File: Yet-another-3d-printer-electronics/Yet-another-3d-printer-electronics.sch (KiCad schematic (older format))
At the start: 118 parts, among them CON1 SD_Card, P1 USB_B, P2 BEDTEMP, P3 ENDTEMP, P4 X-ENDSTOP, P5 Y-ENDSTOP, P6 Z-ENDSTOP, SW1 Switch_DPST, U1 FT230XS, U2 LPC1114FBD48/302, X1 CRYSTAL_SMD

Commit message: Update schematics and pro file
Signed-off-by: Mateusz Krawczuk <mat.krawczuk@gmail.com>
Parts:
- removed Q?: 2N7000, symbol Q_NMOS_GDS
- added Q1: 2N7000, TO_SOT_Packages_THT:TO-92_Horizontal1_Inline_Narrow_Oval, symbol Q_NMOS_SGD
- 100K1: renamed from 100K; footprint (none) -> Resistors_SMD:R_0805_HandSoldering
- 100K2, 100K3, 100K4: renamed from 100K?; footprint (none) -> Resistors_SMD:R_0805_HandSoldering
- C10, C11, C12, C9: renamed from C?; footprint (none) -> Capacitors_THT:CP_Radial_D5.0mm_P2.00mm
- C13: renamed from 10u/30V; value C -> 10u/30V; footprint (none) -> Capacitors_SMD:C_1206_HandSoldering
- C14, C15, C16: renamed from 10u/30V?; value C -> 10u/30V; footprint (none) -> Capacitors_SMD:C_1206_HandSoldering
- D1, D2: symbol LED -> LED-RESCUE-Yet-another-3d-printer-electronics
- D10, D4, D6, D8: renamed from D?; footprint (none) -> Diodes_THT:D_DO-41_SOD81_P2.54mm_Vertical_AnodeUp
- D11, D12, D13, D14, D15, D16, D17, D18, D19, D20, D21, D22, D23, D24, D25, D26, D27, D28, D29, D30, D31, D32, D33, D34, D35, D36, D37, D38, D39, D40, D41, D42: renamed from D?; footprint (none) -> Yet-another-3d-printer-electronics:DO-214AC(SMA)
- D3, D5, D7, D9: renamed from D?; footprint (none) -> LEDs:LED_0805; symbol LED -> LED-RESCUE-Yet-another-3d-printer-electronics
- P1: symbol USB_B -> USB_B-RESCUE-Yet-another-3d-printer-electronics
- P10, P12: renamed from P?; footprint (none) -> Connectors_JST:JST_XH_B02B-XH-A_02x2.50mm_Straight
- P11, P13, P14, P9: renamed from P?; footprint (none) -> Socket_Strips:Socket_Strip_Straight_2x03_Pitch2.54mm
- P15, P16, P17, P18: renamed from P?; footprint (none) -> Connectors_JST:JST_XH_B04B-XH-A_04x2.50mm_Straight
- P2, P3: footprint Socket_Strips:Socket_Strip_Straight_1x02 -> Connectors_JST:JST_XH_B02B-XH-A_02x2.50mm_Straight
- P4, P5, P6: footprint Socket_Strips:Socket_Strip_Straight_1x03 -> Connectors_JST:JST_XH_B03B-XH-A_03x2.50mm_Straight
- P7, P8: renamed from P?; footprint (none) -> Connectors:AK300-2
- Q2, Q4: renamed from Q?; footprint (none) -> TO_SOT_Packages_SMD:TO-252-2Lead
- Q3, Q5: renamed from Q?; footprint (none) -> TO_SOT_Packages_SMD:SOT-23
- R10, R11, R12, R13, R14, R15, R16, R17, R18, R19, R20, R21, R22, R23, R8, R9: renamed from R?; footprint (none) -> Resistors_SMD:R_0805_HandSoldering
- U3, U4, U5, U6: renamed from U?; footprint (none) -> Yet-another-3d-printer-electronics:stepstick_socket
- X1: footprint (none) -> Crystals:Crystal_SMD_HC49-SD_HandSoldering
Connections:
- net FAN: now also R17.2, R18.1; no longer R17.1, R18.2
- net GND: now also Q5.2 (S), R18.2, Q1.1 (S); no longer Q5.3 (D), R18.1
- net at Q2.1 (G), R10.1: now also Q1.3 (D)
- net at R9.1: now also Q1.2 (G)
- net at D10.2 (A), D9.1 (K), P12.1 (P1): now also Q5.3 (D); no longer Q5.2 (S)
- net at Q5.1 (G): now also R17.1; no longer R17.2
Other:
- moved on the sheet: D10, D9, P12, Q5, R17, R18, R19

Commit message: Move FTDI, Stepstick,Heaters and Fan to hierarchical schematics
Signed-off-by: Mateusz Krawczuk <mat.krawczuk@gmail.com>
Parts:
- removed 100K1, 100K2, 100K3, 100K4, R11, R15, R16, R19: R, Resistors_SMD:R_0805_HandSoldering, symbol R
- removed C10, C11, C12, C9: CP, Capacitors_THT:CP_Radial_D5.0mm_P2.00mm, symbol CP
- removed C13, C14, C15, C16: 10u/30V, Capacitors_SMD:C_1206_HandSoldering, symbol C
- removed C2: 100nF, Capacitors_SMD:C_0805_HandSoldering, symbol C
- removed C3, C4: 47pF, Capacitors_SMD:C_0805_HandSoldering, symbol C
- removed C6: 10nF, Capacitors_SMD:C_0805_HandSoldering, symbol C
- removed D1, D2, D3, D5, D7, D9: LED, LEDs:LED_0805, symbol LED-RESCUE-Yet-another-3d-printer-electronics
- removed D10, D4, D6, D8: D, Diodes_THT:D_DO-41_SOD81_P2.54mm_Vertical_AnodeUp, symbol D
- removed D11, D12, D13, D14, D15, D16, D17, D18, D19, D20, D21, D22, D23, D24, D25, D26, D27, D28, D29, D30, D31, D32, D33, D34, D35, D36, D37, D38, D39, D40, D41, D42: D_Schottky, Yet-another-3d-printer-electronics:DO-214AC(SMA), symbol D_Schottky
- removed L1: Ferrite Bead, Choke_SMD:Choke_SMD_Wuerth-WE-PDF_Handsoldering, symbol INDUCTOR
- removed P1: USB_B, Connect:USB_B, symbol USB_B-RESCUE-Yet-another-3d-printer-electronics
- removed P10: HEATER_FAN, Connectors_JST:JST_XH_B02B-XH-A_02x2.50mm_Straight, symbol CONN_01X02
- removed P11: Y-microsteps, Socket_Strips:Socket_Strip_Straight_2x03_Pitch2.54mm, symbol CONN_02X03
- removed P12: FAN, Connectors_JST:JST_XH_B02B-XH-A_02x2.50mm_Straight, symbol CONN_01X02
- removed P13: Z-microsteps, Socket_Strips:Socket_Strip_Straight_2x03_Pitch2.54mm, symbol CONN_02X03
- removed P14: E-microsteps, Socket_Strips:Socket_Strip_Straight_2x03_Pitch2.54mm, symbol CONN_02X03
- removed P15: X-Motor, Connectors_JST:JST_XH_B04B-XH-A_04x2.50mm_Straight, symbol CONN_01X04
- removed P16: Y-Motor, Connectors_JST:JST_XH_B04B-XH-A_04x2.50mm_Straight, symbol CONN_01X04
- removed P17, P18: Z-Motor, Connectors_JST:JST_XH_B04B-XH-A_04x2.50mm_Straight, symbol CONN_01X04
- removed P7: HEATER_BED, Connectors:AK300-2, symbol CONN_01X02
- removed P8: HEATER_EXT, Connectors:AK300-2, symbol CONN_01X02
- removed P9: X-microsteps, Socket_Strips:Socket_Strip_Straight_2x03_Pitch2.54mm, symbol CONN_02X03
- removed Q1: 2N7000, TO_SOT_Packages_THT:TO-92_Horizontal1_Inline_Narrow_Oval, symbol Q_NMOS_SGD
- removed Q2, Q4: IRLR8743PBF, TO_SOT_Packages_SMD:TO-252-2Lead, symbol Q_NMOS_GDS
- removed Q3, Q5: IRLML0030TRPBF, TO_SOT_Packages_SMD:SOT-23, symbol Q_NMOS_GSD
- removed R10, R14, R20, R21, R22, R23: 10K, Resistors_SMD:R_0805_HandSoldering, symbol R
- removed R12, R17, R8: 1M, Resistors_SMD:R_0805_HandSoldering, symbol R
- removed R13, R18, R9: 10R, Resistors_SMD:R_0805_HandSoldering, symbol R
- removed R3, R4, R5, R6: 27R, Resistors_SMD:R_0805_HandSoldering, symbol R
- removed U1: FT230XS, Housings_SSOP:SSOP-16_3.9x4.9mm_Pitch0.635mm, symbol FT230XS
- removed U3: X-Stepstick, Yet-another-3d-printer-electronics:stepstick_socket, symbol StepStick
- removed U4: Y-Stepstick, Yet-another-3d-printer-electronics:stepstick_socket, symbol StepStick
- removed U5: Z-Stepstick, Yet-another-3d-printer-electronics:stepstick_socket, symbol StepStick
- removed U6: E-Stepstick, Yet-another-3d-printer-electronics:stepstick_socket, symbol StepStick
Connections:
- net Stepstick/Z-STEP: now reaches U2.1 (PIO2_6)
- net Stepstick/Z-DIR: now reaches U2.11 (PIO2_7)
- net Stepstick/Y-STEP: now reaches U2.12 (PIO2_8)
- net Stepstick/Z_ENABLE: now reaches U2.13 (PIO2_1/~DSR~/SCK1)
- net Stepstick/XYE_ENABLE: now reaches U2.2 (PIO2_0/~DTR~/SSEL1)
- net Stepstick/Y-DIR: now reaches U2.24 (PIO2_9)
- net Stepstick/E-STEP: now reaches U2.25 (PIO2_10)
- net Stepstick/X-STEP: now reaches U2.26 (PIO2_2/~DCD~/MISO1)
- net Stepstick/E-DIR: now reaches U2.31 (PIO2_11/SCK0)
- net Heaters_and_fan/FAN: now reaches U2.36 (PIO3_0/~DTR~)
- net Heaters_and_fan/HEAT_EXT: now reaches U2.37 (PIO3_1/~DSR~)
- net Stepstick/X-DIR: now reaches U2.38 (PIO2_3/~RI~/MOSI1)
- net Heaters_and_fan/HEAT_BED: now reaches U2.43 (PIO3_2/~DCD~)
- net UART_RX renamed USB_FTDI_UART/UART_RX
- net UART_TX renamed USB_FTDI_UART/UART_TX
- no-connect marks 8 -> 3
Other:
- moved on the sheet: C7, C8, R7, SW1, U2, X1

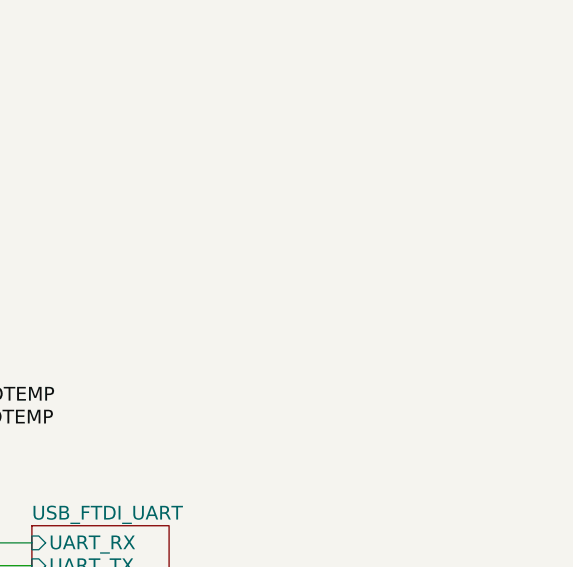
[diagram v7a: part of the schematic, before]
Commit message: Add power section and remove fan heater
Add aoz1284pi buck conventer.

Signed-off-by: Mateusz Krawczuk <mat.krawczuk@gmail.com>
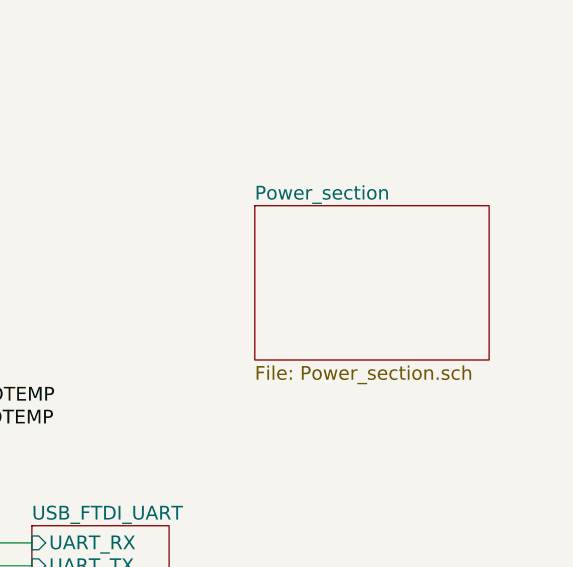
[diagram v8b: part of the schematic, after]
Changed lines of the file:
@@
 LIBS:valves
 LIBS:ftdi
+LIBS:aoz1284pi
 LIBS:Yet-another-3d-printer-electronics-cache
 EELAYER 25 0
@@
 $Descr A4 11693 8268
 encoding utf-8
-Sheet 1 4
+Sheet 1 5
 Title "ZeroBoard - working title"
 Date "2017-02-24"
@@
 $EndComp
 $Comp
-L GND #PWR014
+L GND #PWR07
 U 1 1 588E214E
 P 1200 1525
-F 0 "#PWR014" H 1200 1275 50  0001 C CNN
+F 0 "#PWR07" H 1200 1275 50  0001 C CNN
 F 1 "GND" H 1200 1375 50  0000 C CNN
 F 2 "" H 1200 1525 50  0000 C CNN
@@
 $EndComp
 $Comp
-L VCC #PWR015
+L VCC #PWR08
 U 1 1 588E231C
 P 1025 750
-F 0 "#PWR015" H 1025 600 50  0001 C CNN
+F 0 "#PWR08" H 1025 600 50  0001 C CNN
 F 1 "VCC" H 1025 900 50  0000 C CNN
 F 2 "" H 1025 750 50  0000 C CNN
@@
 $EndComp
 $Comp
-L GND #PWR016
+L GND #PWR09
 U 1 1 588E3505
 P 2300 1525
-F 0 "#PWR016" H 2300 1275 50  0001 C CNN
+F 0 "#PWR09" H 2300 1275 50  0001 C CNN
 F 1 "GND" H 2300 1375 50  0000 C CNN
 F 2 "" H 2300 1525 50  0000 C CNN
@@
 $EndComp
 $Comp
-L VCC #PWR017
+L VCC #PWR010
 U 1 1 588E3510
 P 2125 750
-F 0 "#PWR017" H 2125 600 50  0001 C CNN
+F 0 "#PWR010" H 2125 600 50  0001 C CNN
 F 1 "VCC" H 2125 900 50  0000 C CNN
 F 2 "" H 2125 750 50  0000 C CNN
@@
 $EndComp
 $Comp
-L GND #PWR018
+L GND #PWR011
 U 1 1 588EBC43
 P 3225 1025
-F 0 "#PWR018" H 3225 775 50  0001 C CNN
+F 0 "#PWR011" H 3225 775 50  0001 C CNN
 F 1 "GND" H 3225 875 50  0000 C CNN
 F 2 "" H 3225 1025 50  0000 C CNN
@@
 $EndComp
 $Comp
-L VCC #PWR019
+L VCC #PWR012
 U 1 1 588ECE1F
 P 4700 1125
-F 0 "#PWR019" H 4700 975 50  0001 C CNN
+F 0 "#PWR012" H 4700 975 50  0001 C CNN
 F 1 "VCC" H 4700 1275 50  0000 C CNN
 F 2 "" H 4700 1125 50  0000 C CNN
@@
 NoConn ~ 3050 6475
 $Comp
-L GND #PWR020
+L GND #PWR013
 U 1 1 588EF0E4
 P 3100 6900
-F 0 "#PWR020" H 3100 6650 50  0001 C CNN
+F 0 "#PWR013" H 3100 6650 50  0001 C CNN
 F 1 "GND" H 3100 6750 50  0000 C CNN
 F 2 "" H 3100 6900 50  0000 C CNN
@@
 $EndComp
 $Comp
-L GND #PWR034
+L GND #PWR014
 U 1 1 5890B49A
 P 1200 6475
-F 0 "#PWR034" H 1200 6225 50  0001 C CNN
+F 0 "#PWR014" H 1200 6225 50  0001 C CNN
 F 1 "GND" V 1200 6275 50  0000 C CNN
 F 2 "" H 1200 6475 50  0000 C CNN
@@
 $EndComp
 $Comp
-L VCC #PWR035
+L VCC #PWR015
 U 1 1 5890C3D7
 P 1200 6575
-F 0 "#PWR035" H 1200 6425 50  0001 C CNN
+F 0 "#PWR015" H 1200 6425 50  0001 C CNN
 F 1 "VCC" V 1200 6775 50  0000 C CNN
 F 2 "" H 1200 6575 50  0000 C CNN
@@
 SD-SS
 $Comp
-L GND #PWR036
+L GND #PWR016
 U 1 1 5890D76C
 P 1200 6775
-F 0 "#PWR036" H 1200 6525 50  0001 C CNN
+F 0 "#PWR016" H 1200 6525 50  0001 C CNN
 F 1 "GND" V 1200 6575 50  0000 C CNN
 F 2 "" H 1200 6775 50  0000 C CNN
@@
 Wire Wire Line
 	3675 4075 4475 4075
+$Sheet
+S 8150 1750 1025 675
+U 58B10119
+F0 "Power_section" 60
+F1 "Power_section.sch" 60
+$EndSheet
 $EndSCHEMATC
